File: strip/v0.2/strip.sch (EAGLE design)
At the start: 96 parts, among them IC1 LP2992, IC2 AUIRS2184S, IC3 MAX3051, IC4 OPA335, IC5 AUIRS2184S, IC6 AUIRS2184S, IC7 STM32F050CX, Q1 IRF7828, Q2 IRF7828, Q3 IRF7828, Q4 IRF7828, Q5 IRF7828, Q6 IRF7828

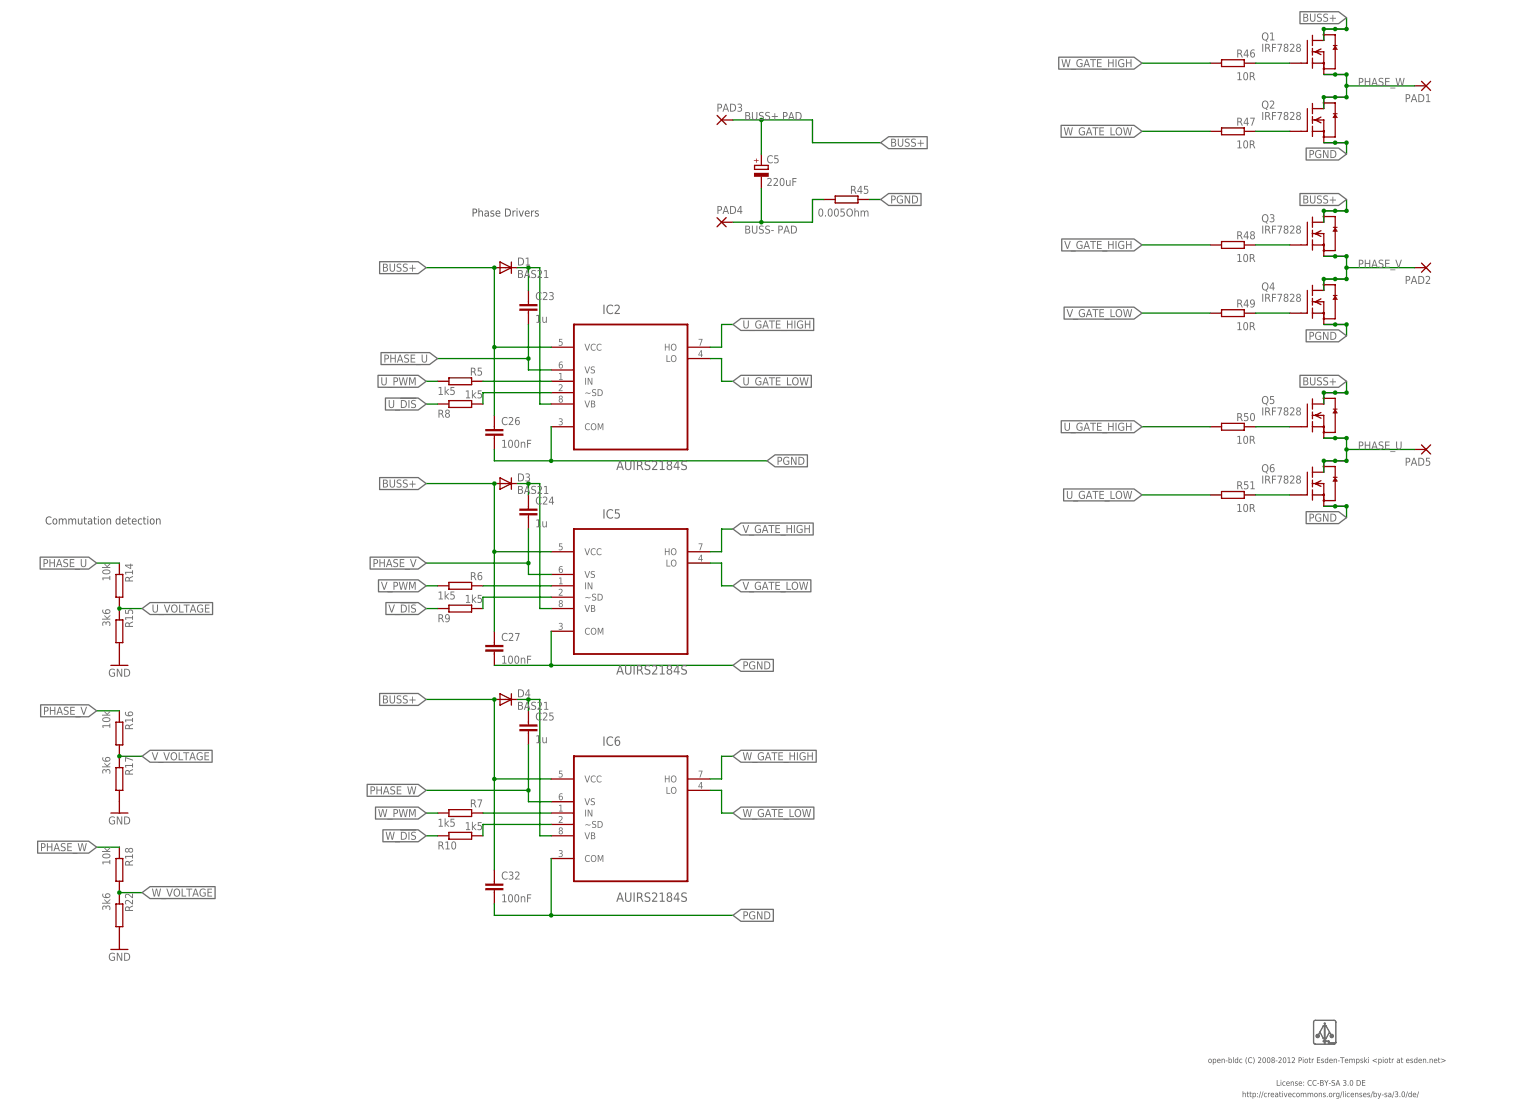
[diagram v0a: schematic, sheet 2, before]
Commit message: Updated bootstrap circuit.
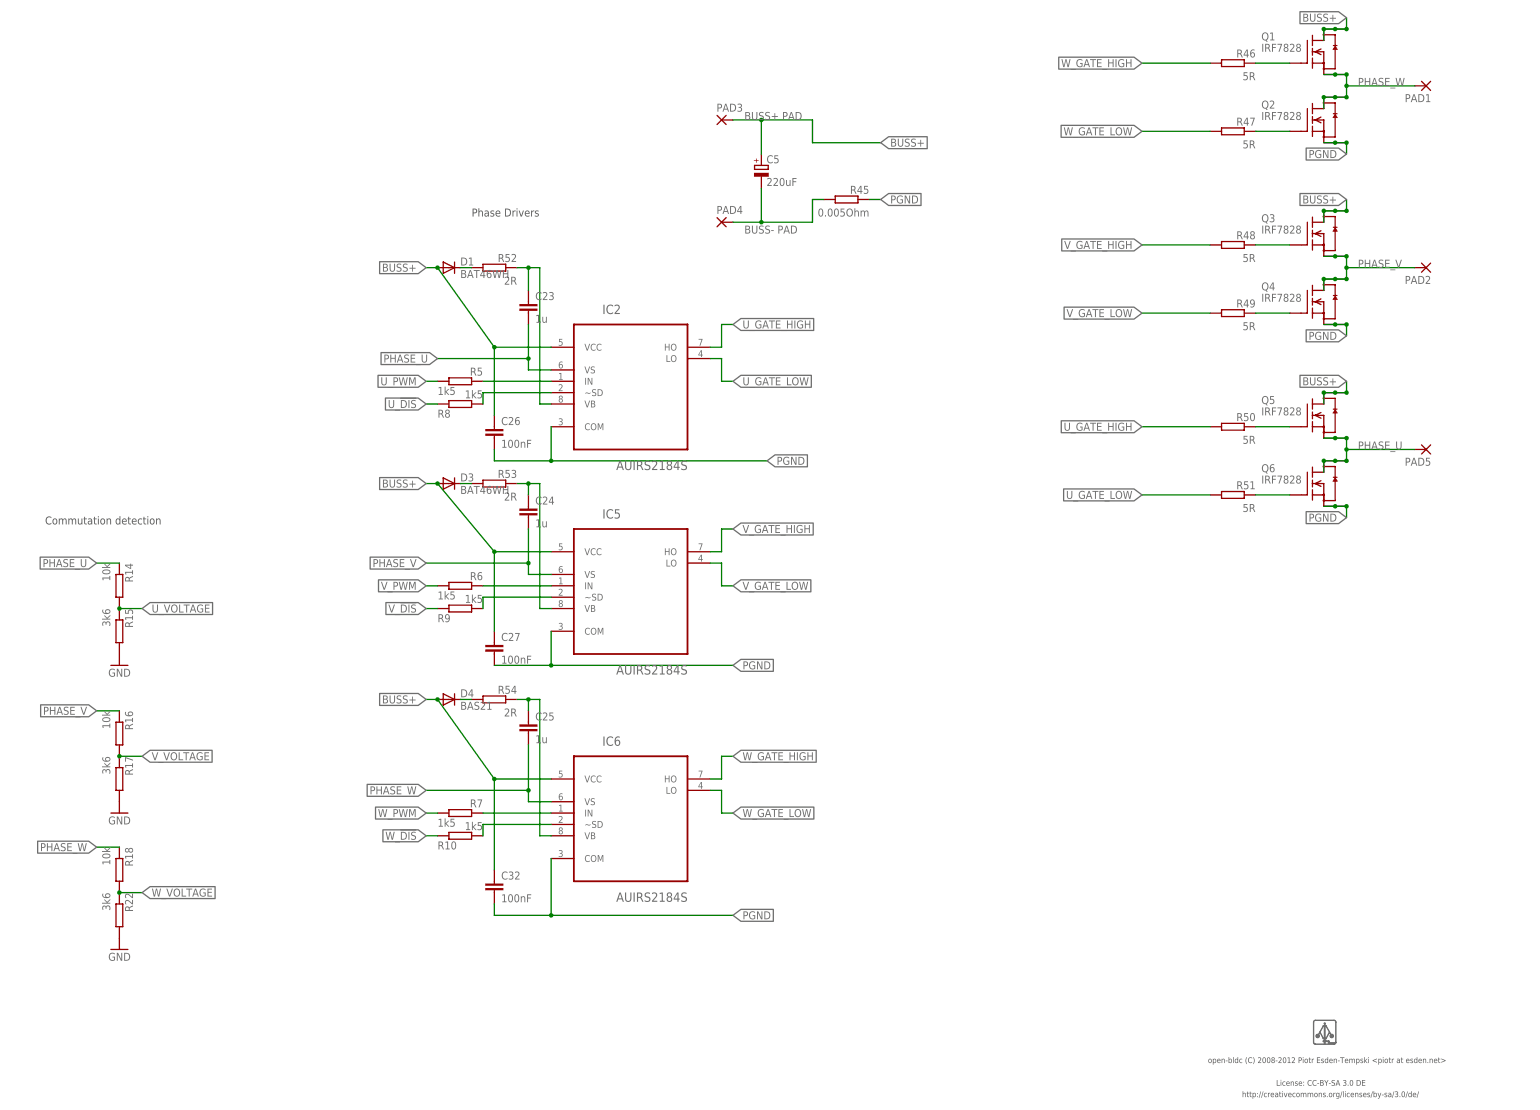
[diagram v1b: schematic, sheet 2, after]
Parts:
- added R52, R53, R54: 2R, pel_dipol_comp:RESISTOR-0402
- D1, D3: value BAS21 -> BAT46WH
- R46, R47, R48, R49, R50, R51: value 10R -> 5R
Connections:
- new net N$1: D1.C, R52.2
- new net N$2: D4.C, R54.2
- new net N$3: D3.C, R53.2
- net U_VB: now also R52.1; no longer D1.C
- net V_VB: now also R53.1; no longer D3.C
- net W_VB: now also R54.1; no longer D4.C
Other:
- moved on the sheet: D1, D3, D4
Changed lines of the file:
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@@
 <part name="GND30" library="supply1" deviceset="GND" device=""/>
 <part name="FRAME2" library="frames" deviceset="A3L-LOC" device=""/>
-<part name="D1" library="pel_dipol_comp" deviceset="DIODE" device="-SOD-123" value="BAS21">
+<part name="D1" library="pel_dipol_comp" deviceset="DIODE" device="-SOD-123" value="BAT46WH">
 <attribute name="PARTNO" value="*"/>
 </part>
@@
 </part>
 <part name="GND7" library="supply1" deviceset="GND" device=""/>
-<part name="D3" library="pel_dipol_comp" deviceset="DIODE" device="-SOD-123" value="BAS21">
+<part name="D3" library="pel_dipol_comp" deviceset="DIODE" device="-SOD-123" value="BAT46WH">
 <attribute name="PARTNO" value="*"/>
 </part>
@@
 <attribute name="PARTNO" value="res-1206-0005"/>
 </part>
-<part name="R46" library="pel_dipol_comp" deviceset="RESISTOR" device="-0603" value="10R">
+<part name="R46" library="pel_dipol_comp" deviceset="RESISTOR" device="-0603" value="5R">
 <attribute name="PARTNO" value="res-0402-10"/>
 </part>
-<part name="R47" library="pel_dipol_comp" deviceset="RESISTOR" device="-0603" value="10R">
+<part name="R47" library="pel_dipol_comp" deviceset="RESISTOR" device="-0603" value="5R">
 <attribute name="PARTNO" value="res-0402-10"/>
 </part>
-<part name="R48" library="pel_dipol_comp" deviceset="RESISTOR" device="-0603" value="10R">
+<part name="R48" library="pel_dipol_comp" deviceset="RESISTOR" device="-0603" value="5R">
 <attribute name="PARTNO" value="res-0402-10"/>
 </part>
-<part name="R49" library="pel_dipol_comp" deviceset="RESISTOR" device="-0603" value="10R">
+<part name="R49" library="pel_dipol_comp" deviceset="RESISTOR" device="-0603" value="5R">
 <attribute name="PARTNO" value="res-0402-10"/>
 </part>
-<part name="R50" library="pel_dipol_comp" deviceset="RESISTOR" device="-0603" value="10R">
+<part name="R50" library="pel_dipol_comp" deviceset="RESISTOR" device="-0603" value="5R">
 <attribute name="PARTNO" value="res-0402-10"/>
 </part>
-<part name="R51" library="pel_dipol_comp" deviceset="RESISTOR" device="-0603" value="10R">
+<part name="R51" library="pel_dipol_comp" deviceset="RESISTOR" device="-0603" value="5R">
 <attribute name="PARTNO" value="res-0402-10"/>
 </part>
@@
 <part name="J3" library="pel_jumpers" deviceset="SQ_JMP" device="-0402">
 <attribute name="PARTNO" value="res-0402-0"/>
+</part>
+<part name="R52" library="pel_dipol_comp" deviceset="RESISTOR" device="-0402" value="2R">
+<attribute name="PARTNO" value="res-0402-10"/>
+</part>
+<part name="R53" library="pel_dipol_comp" deviceset="RESISTOR" device="-0402" value="2R">
+<attribute name="PARTNO" value="res-0402-10"/>
+</part>
+<part name="R54" library="pel_dipol_comp" deviceset="RESISTOR" device="-0402" value="2R">
+<attribute name="PARTNO" value="res-0402-10"/>
 </part>
 </parts>
@@
 <instances>
 <instance part="FRAME2" gate="G$1" x="0" y="0"/>
-<instance part="D1" gate="G$1" x="132.08" y="190.5">
-<attribute name="PARTNO" x="132.08" y="190.5" size="1.778" layer="96" rot="R90" display="off"/>
+<instance part="D1" gate="G$1" x="119.38" y="190.5">
+<attribute name="PARTNO" x="119.38" y="190.5" size="1.778" layer="96" rot="R90" display="off"/>
 </instance>
 <instance part="C23" gate="G$1" x="137.16" y="182.88">
 <attribute name="PARTNO" x="137.16" y="182.88" size="1.778" layer="96" rot="R180" display="off"/>
 </instance>
-<instance part="D3" gate="G$1" x="132.08" y="142.24">
-<attribute name="PARTNO" x="132.08" y="142.24" size="1.778" layer="96" rot="R90" display="off"/>
+<instance part="D3" gate="G$1" x="119.38" y="142.24">
+<attribute name="PARTNO" x="119.38" y="142.24" size="1.778" layer="96" rot="R90" display="off"/>
 </instance>
 <instance part="C24" gate="G$1" x="137.16" y="137.16">
 <attribute name="PARTNO" x="137.16" y="137.16" size="1.778" layer="96" rot="R180" display="off"/>
 </instance>
-<instance part="D4" gate="G$1" x="132.08" y="93.98">
-<attribute name="PARTNO" x="132.08" y="93.98" size="1.778" layer="96" rot="R90" display="off"/>
+<instance part="D4" gate="G$1" x="119.38" y="93.98">
+<attribute name="PARTNO" x="119.38" y="93.98" size="1.778" layer="96" rot="R90" display="off"/>
 </instance>
 <instance part="C25" gate="G$1" x="137.16" y="88.9">
@@
 <instance part="U$2" gate="G$1" x="315.214" y="19.304">
 <attribute name="PARTNO" x="315.214" y="19.304" size="1.778" layer="96" display="off"/>
+</instance>
+<instance part="R52" gate="G$1" x="129.54" y="190.5" rot="R180">
+<attribute name="PARTNO" x="129.54" y="190.5" size="1.778" layer="96" display="off"/>
+</instance>
+<instance part="R53" gate="G$1" x="129.54" y="142.24" rot="R180">
+<attribute name="PARTNO" x="129.54" y="142.24" size="1.778" layer="96" display="off"/>
+</instance>
+<instance part="R54" gate="G$1" x="129.54" y="93.98" rot="R180">
+<attribute name="PARTNO" x="129.54" y="93.98" size="1.778" layer="96" display="off"/>
 </instance>
 </instances>
@@
 <segment>
 <wire x1="137.16" y1="139.7" x2="137.16" y2="142.24" width="0.1524" layer="91"/>
-<wire x1="134.62" y1="142.24" x2="137.16" y2="142.24" width="0.1524" layer="91"/>
 <pinref part="C24" gate="G$1" pin="1"/>
-<pinref part="D3" gate="G$1" pin="C"/>
-<junction x="137.16" y="142.24"/>
 <pinref part="IC5" gate="A" pin="VB"/>
 <wire x1="142.24" y1="114.3" x2="139.7" y2="114.3" width="0.1524" layer="91"/>
 <wire x1="139.7" y1="114.3" x2="139.7" y2="142.24" width="0.1524" layer="91"/>
 <wire x1="139.7" y1="142.24" x2="137.16" y2="142.24" width="0.1524" layer="91"/>
+<pinref part="R53" gate="G$1" pin="1"/>
+<wire x1="134.62" y1="142.24" x2="137.16" y2="142.24" width="0.1524" layer="91"/>
+<junction x="137.16" y="142.24"/>
 </segment>
 </net>
@@
 <segment>
 <wire x1="137.16" y1="91.44" x2="137.16" y2="93.98" width="0.1524" layer="91"/>
-<wire x1="134.62" y1="93.98" x2="137.16" y2="93.98" width="0.1524" layer="91"/>
 <pinref part="C25" gate="G$1" pin="1"/>
-<pinref part="D4" gate="G$1" pin="C"/>
-<junction x="137.16" y="93.98"/>
 <wire x1="137.16" y1="93.98" x2="139.7" y2="93.98" width="0.1524" layer="91"/>
 <wire x1="139.7" y1="93.98" x2="139.7" y2="63.5" width="0.1524" layer="91"/>
 <pinref part="IC6" gate="A" pin="VB"/>
 <wire x1="139.7" y1="63.5" x2="142.24" y2="63.5" width="0.1524" layer="91"/>
+<pinref part="R54" gate="G$1" pin="1"/>
+<wire x1="134.62" y1="93.98" x2="137.16" y2="93.98" width="0.1524" layer="91"/>
+<junction x="137.16" y="93.98"/>
 </segment>
 </net>
@@
 </segment>
 <segment>
-<wire x1="114.3" y1="190.5" x2="129.54" y2="190.5" width="0.1524" layer="91"/>
-<junction x="129.54" y="190.5"/>
+<wire x1="114.3" y1="190.5" x2="116.84" y2="190.5" width="0.1524" layer="91"/>
+<junction x="116.84" y="190.5"/>
 <pinref part="D1" gate="G$1" pin="A"/>
 <label x="114.3" y="190.5" size="1.778" layer="95" rot="R180" xref="yes"/>
@@
 <pinref part="C26" gate="G$1" pin="1"/>
 <junction x="129.54" y="172.72"/>
-<wire x1="129.54" y1="172.72" x2="129.54" y2="190.5" width="0.1524" layer="91"/>
+<wire x1="129.54" y1="172.72" x2="116.84" y2="190.5" width="0.1524" layer="91"/>
 <pinref part="IC2" gate="A" pin="VCC"/>
 </segment>
 <segment>
-<wire x1="114.3" y1="142.24" x2="129.54" y2="142.24" width="0.1524" layer="91"/>
+<wire x1="114.3" y1="142.24" x2="116.84" y2="142.24" width="0.1524" layer="91"/>
 <wire x1="129.54" y1="109.22" x2="129.54" y2="127" width="0.1524" layer="91"/>
-<junction x="129.54" y="142.24"/>
+<junction x="116.84" y="142.24"/>
 <pinref part="D3" gate="G$1" pin="A"/>
 <label x="114.3" y="142.24" size="1.778" layer="95" rot="R180" xref="yes"/>
 <pinref part="C27" gate="G$1" pin="1"/>
 <junction x="129.54" y="127"/>
-<wire x1="129.54" y1="127" x2="129.54" y2="142.24" width="0.1524" layer="91"/>
+<wire x1="129.54" y1="127" x2="116.84" y2="142.24" width="0.1524" layer="91"/>
 <pinref part="IC5" gate="A" pin="VCC"/>
 <wire x1="142.24" y1="127" x2="129.54" y2="127" width="0.1524" layer="91"/>
 </segment>
 <segment>
-<wire x1="114.3" y1="93.98" x2="129.54" y2="93.98" width="0.1524" layer="91"/>
+<wire x1="114.3" y1="93.98" x2="116.84" y2="93.98" width="0.1524" layer="91"/>
 <wire x1="142.24" y1="76.2" x2="129.54" y2="76.2" width="0.1524" layer="91"/>
-<wire x1="129.54" y1="76.2" x2="129.54" y2="93.98" width="0.1524" layer="91"/>
-<junction x="129.54" y="93.98"/>
+<wire x1="129.54" y1="76.2" x2="116.84" y2="93.98" width="0.1524" layer="91"/>
+<junction x="116.84" y="93.98"/>
 <pinref part="D4" gate="G$1" pin="A"/>
 <pinref part="IC6" gate="A" pin="VCC"/>
@@
 <net name="U_VB" class="0">
 <segment>
-<pinref part="D1" gate="G$1" pin="C"/>
 <pinref part="C23" gate="G$1" pin="1"/>
-<wire x1="134.62" y1="190.5" x2="137.16" y2="190.5" width="0.1524" layer="91"/>
 <wire x1="137.16" y1="190.5" x2="137.16" y2="185.42" width="0.1524" layer="91"/>
-<junction x="137.16" y="190.5"/>
 <wire x1="137.16" y1="190.5" x2="139.7" y2="190.5" width="0.1524" layer="91"/>
 <wire x1="139.7" y1="190.5" x2="139.7" y2="160.02" width="0.1524" layer="91"/>
 <pinref part="IC2" gate="A" pin="VB"/>
 <wire x1="139.7" y1="160.02" x2="142.24" y2="160.02" width="0.1524" layer="91"/>
+<pinref part="R52" gate="G$1" pin="1"/>
+<wire x1="134.62" y1="190.5" x2="137.16" y2="190.5" width="0.1524" layer="91"/>
+<junction x="137.16" y="190.5"/>
 </segment>
 </net>
@@
 </segment>
 </net>
+<net name="N$1" class="0">
+<segment>
+<pinref part="D1" gate="G$1" pin="C"/>
+<pinref part="R52" gate="G$1" pin="2"/>
+<wire x1="121.92" y1="190.5" x2="124.46" y2="190.5" width="0.1524" layer="91"/>
+</segment>
+</net>
+<net name="N$2" class="0">
+<segment>
+<pinref part="D4" gate="G$1" pin="C"/>
+<pinref part="R54" gate="G$1" pin="2"/>
+<wire x1="121.92" y1="93.98" x2="124.46" y2="93.98" width="0.1524" layer="91"/>
+</segment>
+</net>
+<net name="N$3" class="0">
+<segment>
+<pinref part="D3" gate="G$1" pin="C"/>
+<pinref part="R53" gate="G$1" pin="2"/>
+<wire x1="121.92" y1="142.24" x2="124.46" y2="142.24" width="0.1524" layer="91"/>
+</segment>
+</net>
